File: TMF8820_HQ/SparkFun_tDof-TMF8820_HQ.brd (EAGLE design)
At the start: 25.4 x 12.7 mm, 48 parts, among them J4 QWIIC_RIGHT_ANGLE, J5 QWIIC_RIGHT_ANGLE

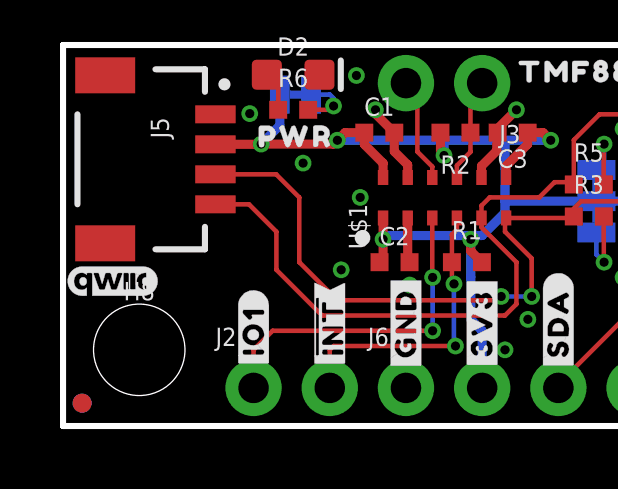
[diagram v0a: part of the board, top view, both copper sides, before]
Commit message: Adds logos to schematic
* Moves measures to board (weren't moved when the design was put at the origin)
* Replaces IO1 silk with IO0 on GPIO0 PTH header
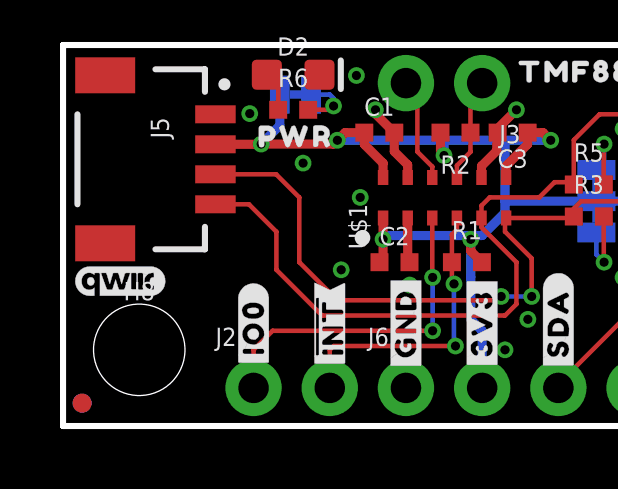
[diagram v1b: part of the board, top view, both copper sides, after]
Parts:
- removed U$36: (no value), SparkFun-Aesthetics:QWIIC_3MM
- added LOGO1: SFE_LOGO_NAMEBLANK, SparkFun-Aesthetics:BLANK
- added LOGO2: QWIIC_LOGO_3MM, SparkFun-Aesthetics:QWIIC_3MM
- added LOGO3: OSHW-LOGONO_SILK, SparkFun-Aesthetics:DUMMY
- U$2: device TMFHQBotSilk:#IO1#8 -> TMFHQTopSilk:#IO0#8
- moved U$2 0.13 mm to (6.35, 3.30)
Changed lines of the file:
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@@
 <wire x1="25.4" y1="0" x2="0" y2="0" width="0.2032" layer="20"/>
 <text x="24.511" y="9.779" size="1.016" layer="16" font="vector" ratio="20" rot="SMR270">v01</text>
-<text x="37.084" y="21.082" size="1.778" layer="47" font="vector">Units in Inches</text>
+<text x="4.064" y="-5.588" size="1.778" layer="47" font="vector">Units in Inches</text>
 <text x="15.367" y="-13.081" size="1.778" layer="51" font="vector">Elias Santistevan</text>
-<dimension x1="33.02" y1="39.37" x2="58.42" y2="39.37" x3="45.72" y3="45.72" textsize="1.778" layer="47" unit="inch"/>
-<dimension x1="33.02" y1="26.67" x2="33.02" y2="39.37" x3="24.13" y3="33.02" textsize="1.778" layer="47" unit="inch"/>
-<dimension x1="38.1" y1="35.56" x2="38.1" y2="26.67" x3="27.94" y3="31.115" textsize="1.778" layer="47" unit="inch"/>
-<dimension x1="45.72" y1="34.29" x2="45.72" y2="26.67" x3="31.75" y3="30.48" textsize="1.778" layer="47" unit="inch"/>
-<dimension x1="55.88" y1="29.21" x2="55.88" y2="26.67" x3="66.04" y3="27.94" textsize="1.778" layer="47" unit="inch"/>
-<dimension x1="55.88" y1="29.21" x2="58.42" y2="29.21" x3="57.15" y3="41.91" textsize="1.778" layer="47" unit="inch"/>
-<dimension x1="45.72" y1="34.29" x2="33.02" y2="34.29" x3="39.37" y3="41.91" textsize="1.778" layer="47" unit="inch"/>
+<dimension x1="0" y1="12.7" x2="25.4" y2="12.7" x3="12.7" y3="19.05" textsize="1.778" layer="47" unit="inch"/>
+<dimension x1="0" y1="0" x2="0" y2="12.7" x3="-8.89" y3="6.35" textsize="1.778" layer="47" unit="inch"/>
+<dimension x1="5.08" y1="8.89" x2="5.08" y2="0" x3="-5.08" y3="4.445" textsize="1.778" layer="47" unit="inch"/>
+<dimension x1="12.7" y1="7.62" x2="12.7" y2="0" x3="-1.27" y3="3.81" textsize="1.778" layer="47" unit="inch"/>
+<dimension x1="22.86" y1="2.54" x2="22.86" y2="0" x3="33.02" y3="1.27" textsize="1.778" layer="47" unit="inch"/>
+<dimension x1="22.86" y1="2.54" x2="25.4" y2="2.54" x3="24.13" y3="15.24" textsize="1.778" layer="47" unit="inch"/>
+<dimension x1="12.7" y1="7.62" x2="0" y2="7.62" x3="6.35" y3="15.24" textsize="1.778" layer="47" unit="inch"/>
 </plain>
 <attributes>
@@
 <element name="U$34" library="SparkFun-Aesthetics" package="OSHW-LOGO-MINI" value="" x="23.749" y="10.922" smashed="yes" rot="MR0"/>
 <element name="U$35" library="SparkFun-Aesthetics" package="SFE_LOGO_FLAME_.1" value="" x="21.082" y="4.318" smashed="yes"/>
-<element name="U$36" library="SparkFun-Aesthetics" package="QWIIC_3MM" value="" x="1.651" y="4.826" smashed="yes"/>
 <element name="U$37" library="TMFHQTopSilk" package="#3V3#0" value="" x="13.97" y="3.429" smashed="yes" rot="R90"/>
 <element name="U$38" library="TMFHQTopSilk" package="#GND#4" value="" x="11.43" y="3.429" smashed="yes" rot="R90"/>
@@
 <element name="U$43" library="TMFHQTopSilk" package="PWR8821882023" value="" x="7.747" y="9.652" smashed="yes"/>
 <element name="U$44" library="TMFHQTopSilk" package="TMF882020" value="" x="17.78" y="11.811" smashed="yes"/>
-<element name="U$2" library="TMFHQBotSilk" package="#IO1#8" value="" x="6.35" y="3.175" smashed="yes" rot="R90"/>
 <element name="U$3" library="TMFHQBotSilk" package="##INT##9" value="" x="8.89" y="3.302" smashed="yes" rot="R90"/>
 <element name="U$4" library="TMFHQTopSilk" package="##INT##8" value="" x="8.89" y="3.302" smashed="yes" rot="MR270"/>
@@
 <element name="U$7" library="TMFHQTopSilk" package="DTOF882188211" value="" x="5.207" y="8.382" smashed="yes" rot="MR0"/>
 <element name="U$8" library="TMFHQTopSilk" package="TMF88209" value="" x="4.953" y="6.985" smashed="yes" rot="MR0"/>
+<element name="LOGO1" library="SparkFun-Aesthetics" package="BLANK" value="SFE_LOGO_NAMEBLANK" x="-11.938" y="-12.954" smashed="yes"/>
+<element name="LOGO2" library="SparkFun-Aesthetics" package="QWIIC_3MM" value="QWIIC_LOGO_3MM" x="1.905" y="4.826" smashed="yes"/>
+<element name="LOGO3" library="SparkFun-Aesthetics" package="DUMMY" value="OSHW-LOGONO_SILK" x="-11.938" y="-12.954" smashed="yes"/>
+<element name="U$2" library="TMFHQTopSilk" package="#IO0#8" value="" x="6.35" y="3.302" smashed="yes" rot="R90"/>
 </elements>
 <signals>

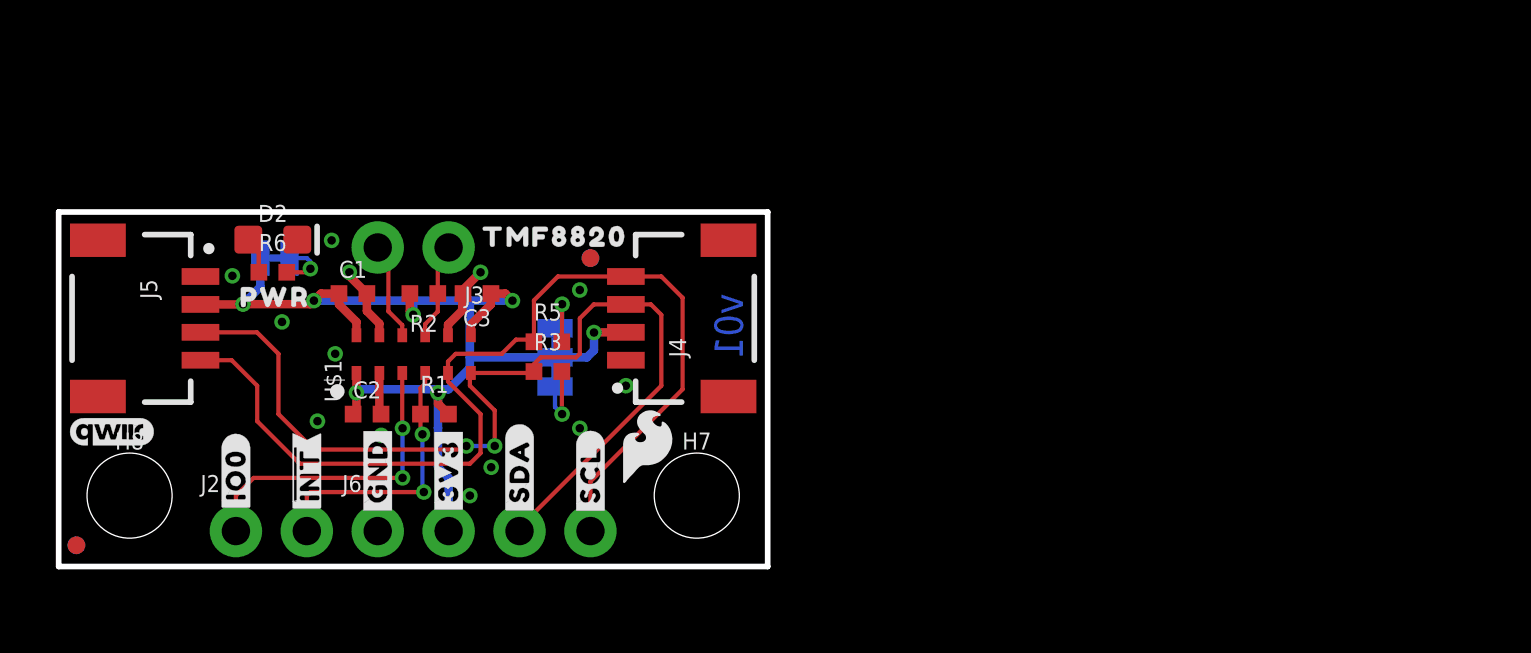
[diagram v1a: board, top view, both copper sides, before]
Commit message: Moves IC to one side and all parts to the other
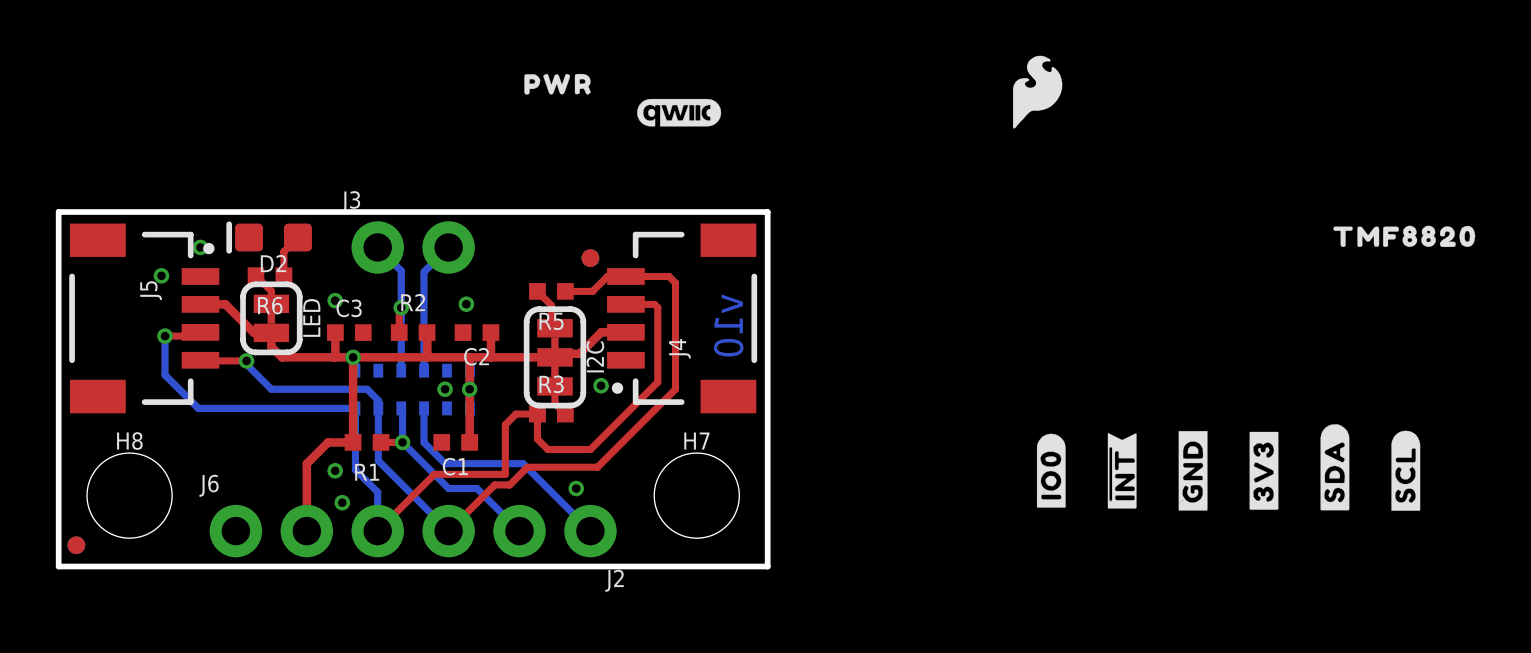
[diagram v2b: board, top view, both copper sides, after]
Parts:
- moved U$44 30.5 mm to (48.3, 11.8)
- moved U$31 29.2 mm to (43.2, 10.9)
- moved U$6 29.2 mm to (40.6, 10.8)
- moved U$5 29.2 mm to (35.6, 3.94)
- moved U$10 29.2 mm to (43.2, 3.43)
- moved U$16 29.2 mm to (40.6, 3.43)
- moved U$2 29.2 mm to (35.6, 3.30)
- moved U$3 29.2 mm to (38.1, 3.30)
- moved U$37 29.2 mm to (43.2, 3.43)
- moved U$38 29.2 mm to (40.6, 3.43)
- moved U$4 29.2 mm to (38.1, 3.30)
- moved U$18 29.2 mm to (45.7, 3.43)
- moved U$19 29.2 mm to (48.3, 3.30)
- moved U$39 29.2 mm to (48.3, 3.30)
- moved U$40 29.2 mm to (45.7, 3.43)
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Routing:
- net 3.3V: track 40.7 -> 31.7 mm, vias 7 -> 2
- net GND: track 6.61 -> 0.00 mm, vias 13 -> 9
- net SCL: track 36.9 -> 31.1 mm, vias 0 -> 1
- net GPIO0/SYNC: track 11.3 -> 8.50 mm, vias 2 -> 0
- net !INT!: track 9.90 -> 7.51 mm, vias 2 -> 1
- net EN: track 3.49 -> 5.68 mm, vias 0 -> 1
- net SDA: track 35.3 -> 33.5 mm, vias 2 -> 1
- net N$7: track 2.62 -> 1.15 mm, vias 1 -> 0
- net GPIO1: track 3.51 -> 4.78 mm
- net N$8: track 2.32 -> 1.58 mm, vias 1 -> 0
- net N$6: track 1.95 -> 1.23 mm, vias 1 -> 0
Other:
- board text added: "v10"
- board text removed: "v01"

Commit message: Moves the IC on the SparkFun "HQ" design to one side
* All other parts are on the other side. This makes room for product selection boxes so that one PCB can be used for both.
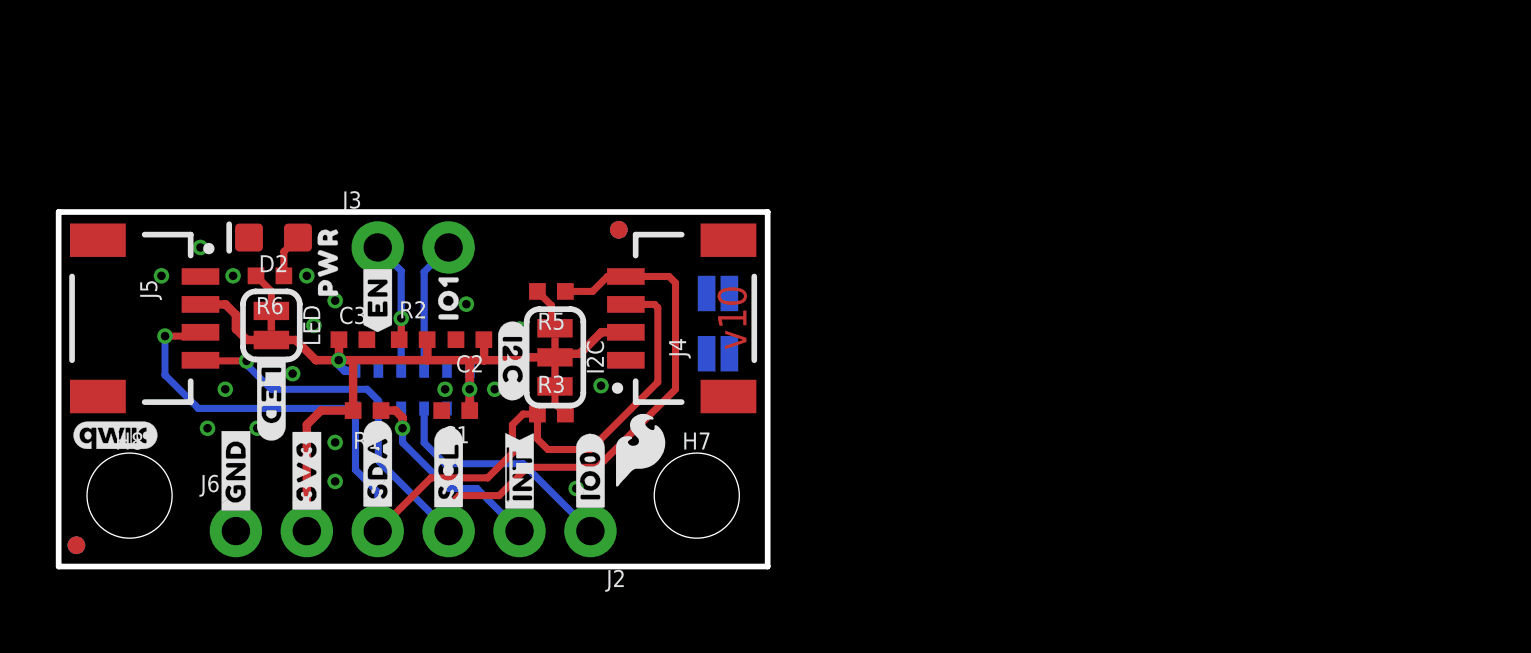
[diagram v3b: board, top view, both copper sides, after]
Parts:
- removed U$34: (no value), SparkFun-Aesthetics:OSHW-LOGO-MINI
- removed U$44: (no value), TMFHQTopSilk:TMF882020
- added TMF8820: JUMPER-SMT_2_NC_PASTE_SILK, SparkFun-Jumpers:SMT-JUMPER_2_NC_PASTE_SILK
- added TMF8821: JUMPER-SMT_2_NO_SILK, SparkFun-Jumpers:SMT-JUMPER_2_NO_SILK
- added U$11: (no value), TMFHQTopSilk:TMF882188210
- added U$12: (no value), TMFMiniTop:IO18
- added U$9: (no value), TMFHQTopSilk:#EN#7
- moved U$18 34.3 mm to (11.4, 3.56)
- moved U$19 34.3 mm to (14.0, 3.43)
- moved U$39 34.3 mm to (14.0, 3.43)
- moved U$40 34.3 mm to (11.4, 3.56)
- moved U$10 34.3 mm to (8.89, 3.43)
- moved U$16 34.3 mm to (6.35, 3.43)
- moved U$37 34.3 mm to (8.89, 3.43)
- moved U$38 34.3 mm to (6.35, 3.43)
- moved U$31 31.8 mm to (11.4, 9.65)
- moved U$33 31.0 mm to (2.16, 8.76)
- moved U$20 26.9 mm to (16.3, 7.37), flipped to the top
- moved U$6 26.7 mm to (14.0, 9.53)
- moved LOGO2 23.3 mm to (2.03, 4.70)
- moved U$3 21.6 mm to (16.5, 3.30)
- moved U$4 21.6 mm to (16.5, 3.30)
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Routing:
- net 3.3V: track 31.7 -> 30.5 mm
- net SCL: track 31.1 -> 31.6 mm
